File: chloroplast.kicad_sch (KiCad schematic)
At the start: 36 parts, among them J3 Pin Header, J4 Pin Header, J5 SWD, J6 USB, J7 Conn_01x02_Socket, J8 Conn_01x04_Socket, J9 I2C, U1 E73-2G4M08S1C, U2 BQ25186DLHR, U3 TPS7A0233PDBVR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

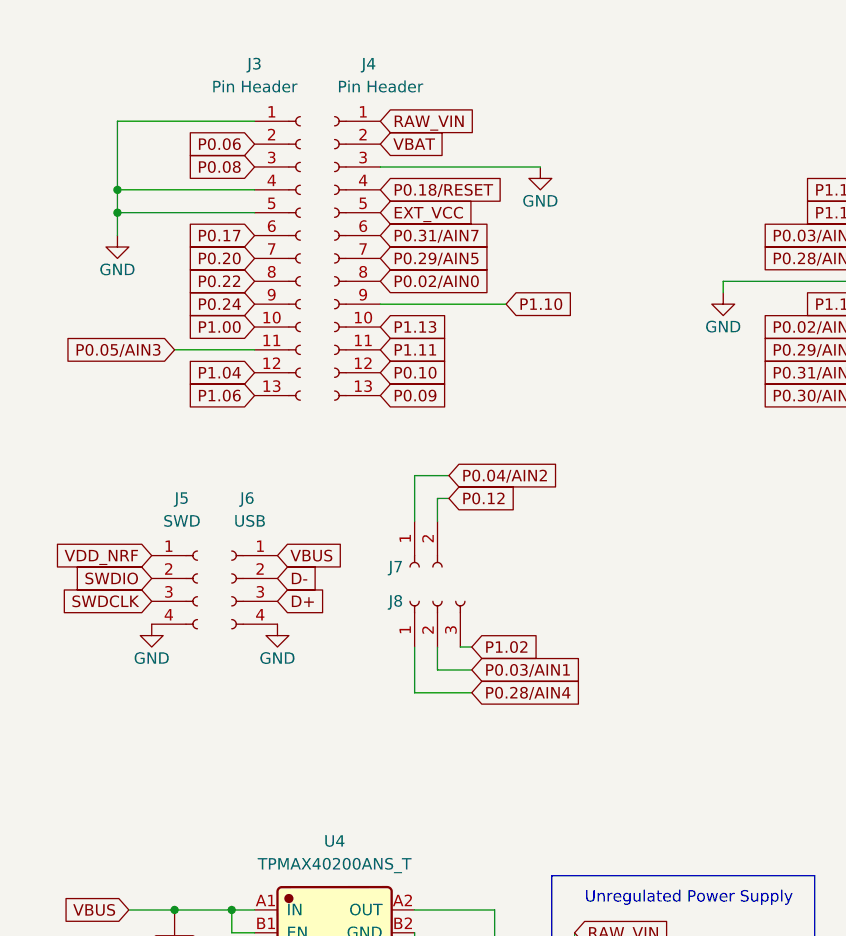
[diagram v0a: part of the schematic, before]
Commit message: add pro-micro pin numbers in schematic
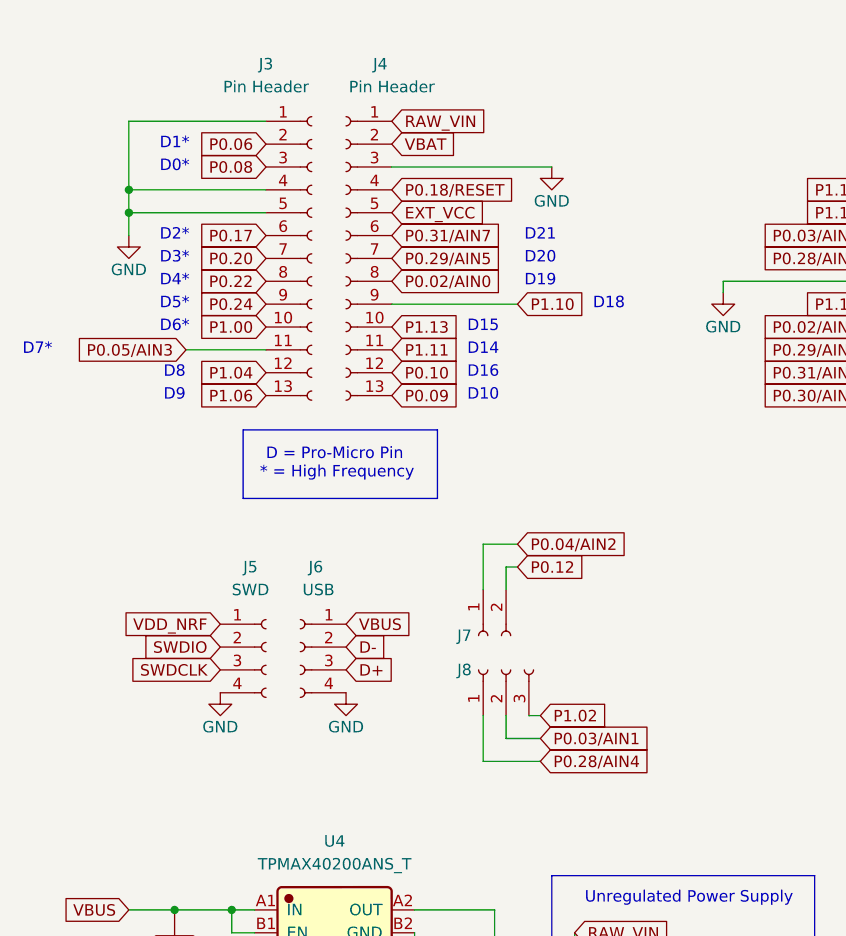
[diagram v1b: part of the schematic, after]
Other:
- note added: "D = Pro-Micro Pin * = High Frequency"
- note added: "D0*"
- note added: "D1*"
- note added: "D10"
- note added: "D14"
- note added: "D15"
- note added: "D16"
- note added: "D18"
- note added: "D19"
- note added: "D2*"
- note added: "D20"
- note added: "D21"
- note added: "D3*"
- note added: "D4*"
- note added: "D5*"
- note added: "D6*"
- note added: "D7*"
- note added: "D8"
- note added: "D9"
- moved on the sheet: J3, J4, J5, J6, J7, J8

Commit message: change L1 to TDK MLZ1608M100WT000
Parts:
- L1: LCSC C109083 -> C76798; Manufacturer FH (Guangdong Fenghua Advanced Tech) -> TDK; Manufacturer Part CMI160808J100KT -> MLZ1608M100WT000
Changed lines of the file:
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@@
 			)
 		)
-		(property "Datasheet" "https://www.lcsc.com/datasheet/lcsc_datasheet_2302231030_FH--Guangdong-Fenghua-Advanced-Tech-CMI160808J100KT_C109083.pdf"
+		(property "Datasheet" "https://www.lcsc.com/datasheet/C76798.pdf"
 			(at 172.72 81.28 0)
 			(effects
@@
 			)
 		)
-		(property "Description" "1.75Ω 10uH 17MHz 20@2MHz 3mA Multilayer inductor、High-frequency inductor ±10% 0603 Inductors (SMD) ROHS"
+		(property "Description" "1.05Ω 10uH 250mA 2MHz 90mA Multilayer inductor ±20% 0603 Inductors (SMD) ROHS"
 			(at 172.72 81.28 0)
 			(effects
@@
 			)
 		)
-		(property "LCSC" "C109083"
+		(property "LCSC" "C76798"
 			(at 172.72 81.28 0)
 			(effects
@@
 			)
 		)
-		(property "Manufacturer" "FH (Guangdong Fenghua Advanced Tech)"
+		(property "Manufacturer" "TDK"
 			(at 172.72 81.28 0)
 			(effects
@@
 			)
 		)
-		(property "Manufacturer Part" "CMI160808J100KT"
+		(property "Manufacturer Part" "MLZ1608M100WT000"
 			(at 172.72 81.28 0)
 			(effects
